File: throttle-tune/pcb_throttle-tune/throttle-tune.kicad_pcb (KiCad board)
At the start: 2 copper layers, 74.7 x 69.1 mm, 51 parts, among them IC1 ATMEGA8A-P, J1 3-speed-IN: COM, sw-fast, sw-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, J10 9V supply batt: GND, 9V, J2 gas-pedal-IN: GND, Analog, 5V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, J3 throttle-OUT: GND, Analog, 5V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, J4 3-speed-OUT: COM, sw-fast, sw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, J5 UART [TX, RX, GND], J7 gpio-reserve, J8 reserve, reverse-sw, J9 5V out, GND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

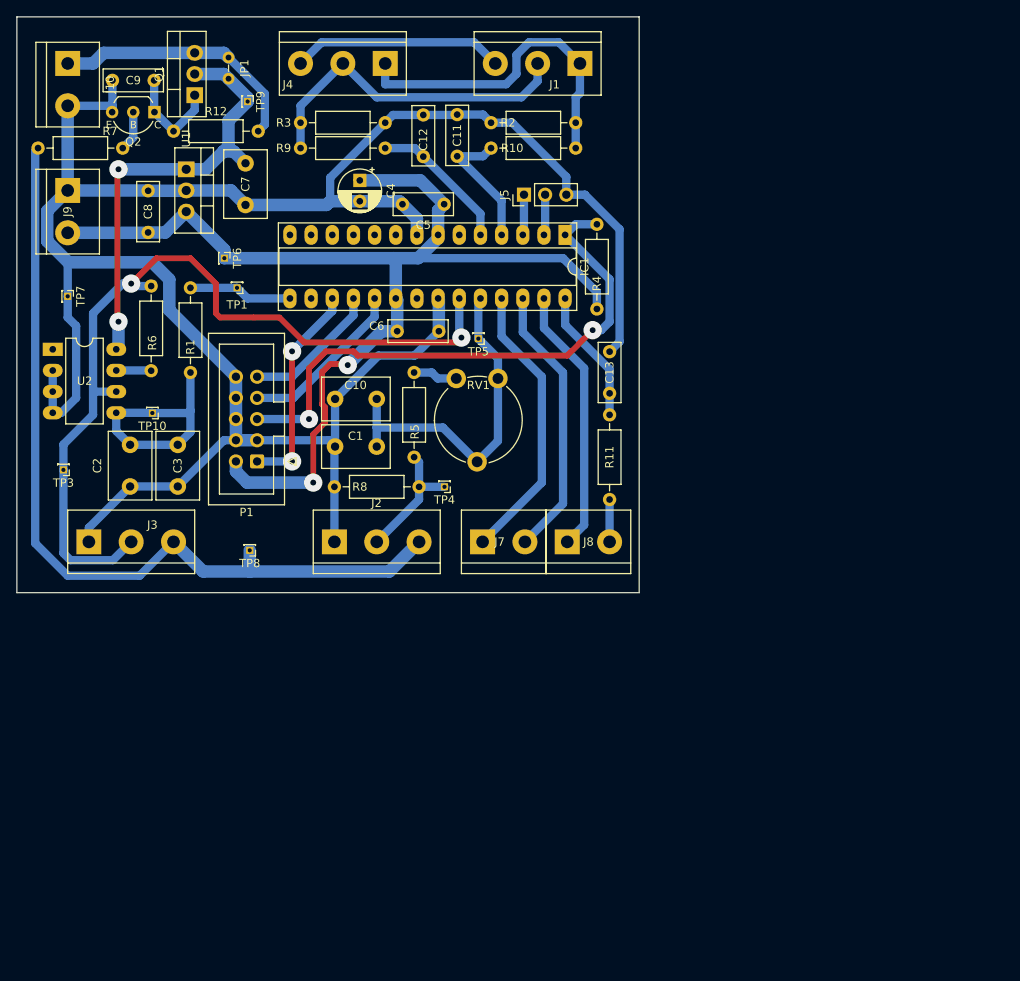
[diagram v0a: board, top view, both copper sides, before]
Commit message: Add text annotations for connecting, Update exports
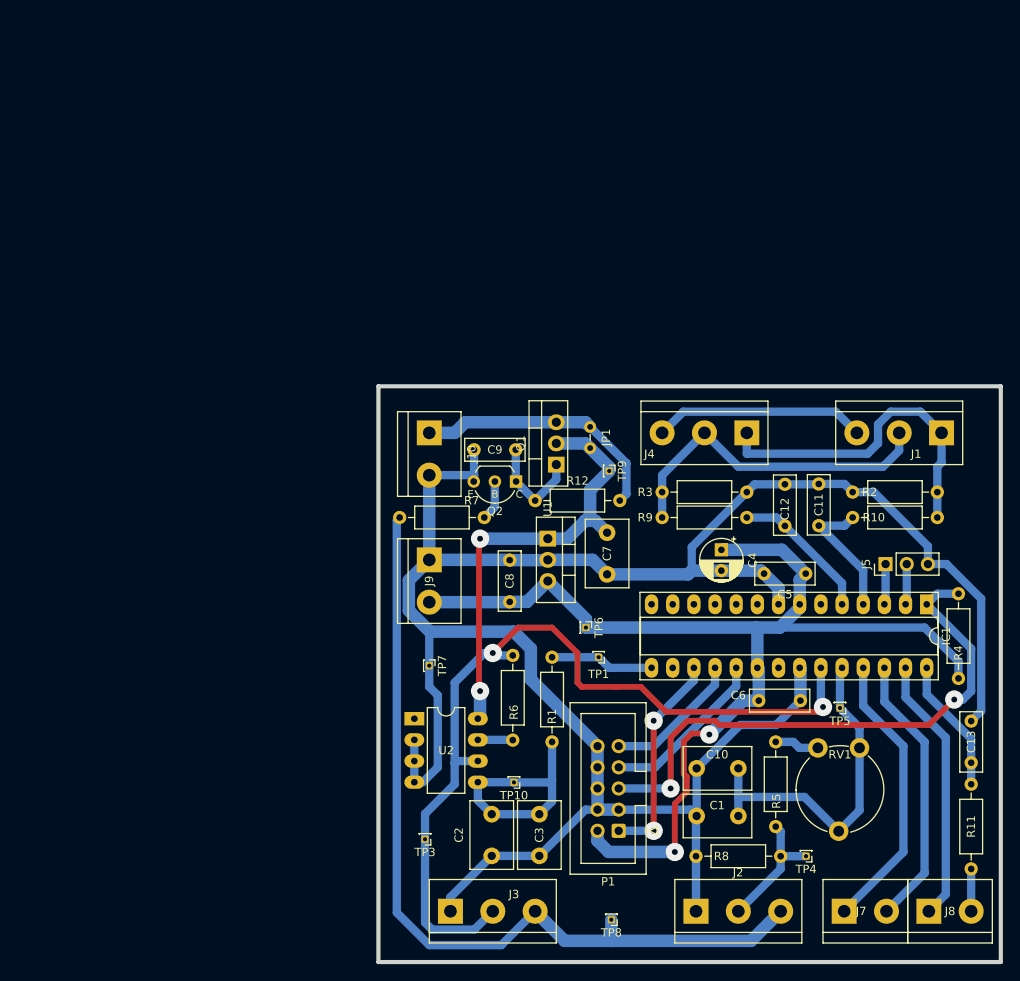
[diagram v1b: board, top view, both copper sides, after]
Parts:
- J8: value reserve, reverse-sw -> reserve, REVERSE-SW
- moved IC1 62.0 mm to (109.2, 70.5)
- moved J3 62.0 mm to (52.0, 107.3)
- moved R10 62.0 mm to (110.4, 60.1)
- moved R9 62.0 mm to (77.4, 60.1)
- moved TP5 62.0 mm to (98.8, 82.9)
- moved TP7 62.0 mm to (49.5, 77.9)
- moved U2 62.0 mm to (47.7, 84.2)
- moved C10 62.0 mm to (86.6, 90.2)
- moved C6 62.0 mm to (89.0, 82.0)
- moved C9 62.0 mm to (59.9, 51.9)
- moved J2 62.0 mm to (81.5, 107.3)
- moved J7 62.0 mm to (99.3, 107.3)
- moved J8 62.0 mm to (109.4, 107.3)
- moved JP1 62.0 mm to (68.8, 49.2)
- moved R11 62.0 mm to (114.5, 102.2)
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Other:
- board text added: "3-speed-switch COM, S1-fast, S2-slow"
- board text added: "9V, GND From 72V to 9V converter"
- board text added: "Adjust Gas-Pedal Lowpass"
- board text added: "GND, Analog, 5V to ESC-throttle-IN"
- board text added: "GND, Analog, 5V to Gas-Pedal-OUT"
- board text added: "Note: connect 5V to 3-speed-sw COM"
- board text added: "PCB: throttle-tune 09.2024"
- board text added: "Reverse Switch: Switch and ESC connected in parallel here switches to GND Pulled up by ESC"
- board text added: "dropped ESC connection here -> connect 3(COM) to 5V (for pullup)"
- board text added: "dropped, motorcontroller (ESC) not connected here"
- board text removed: "dropped (motorcontroller not connected here)"
